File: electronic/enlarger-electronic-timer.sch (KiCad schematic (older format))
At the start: 1 part

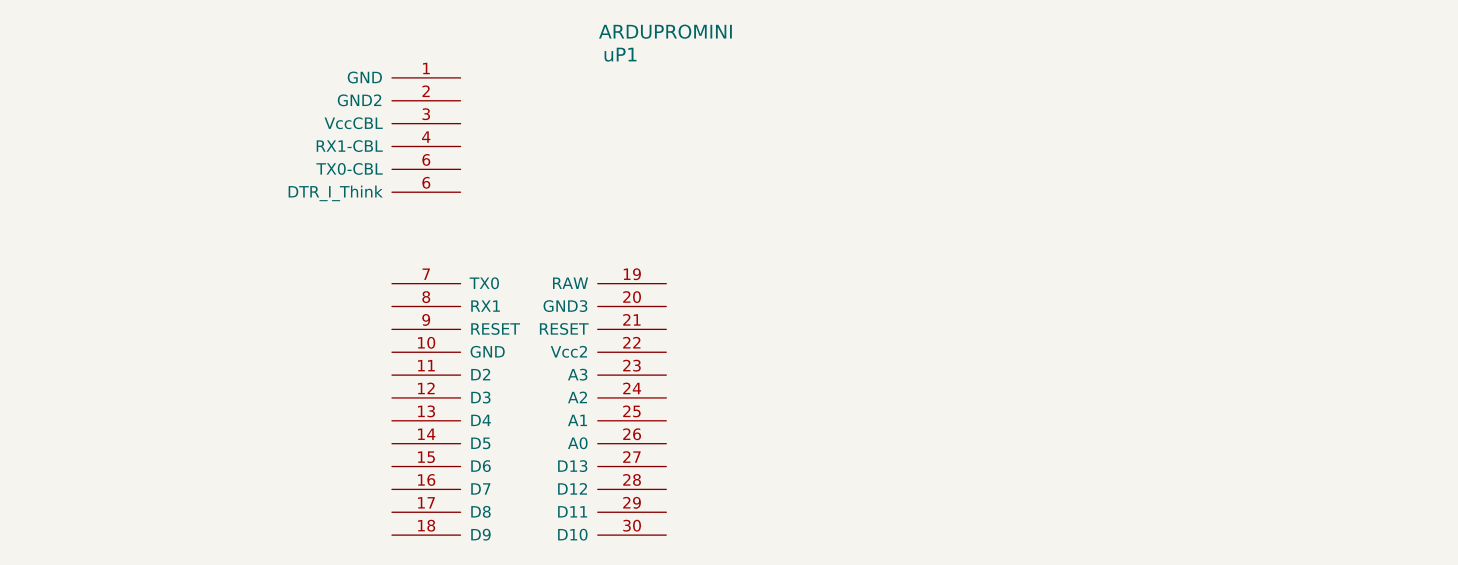
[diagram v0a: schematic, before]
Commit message: Fixed arduino library power pins, added grov connectors for relay/digits
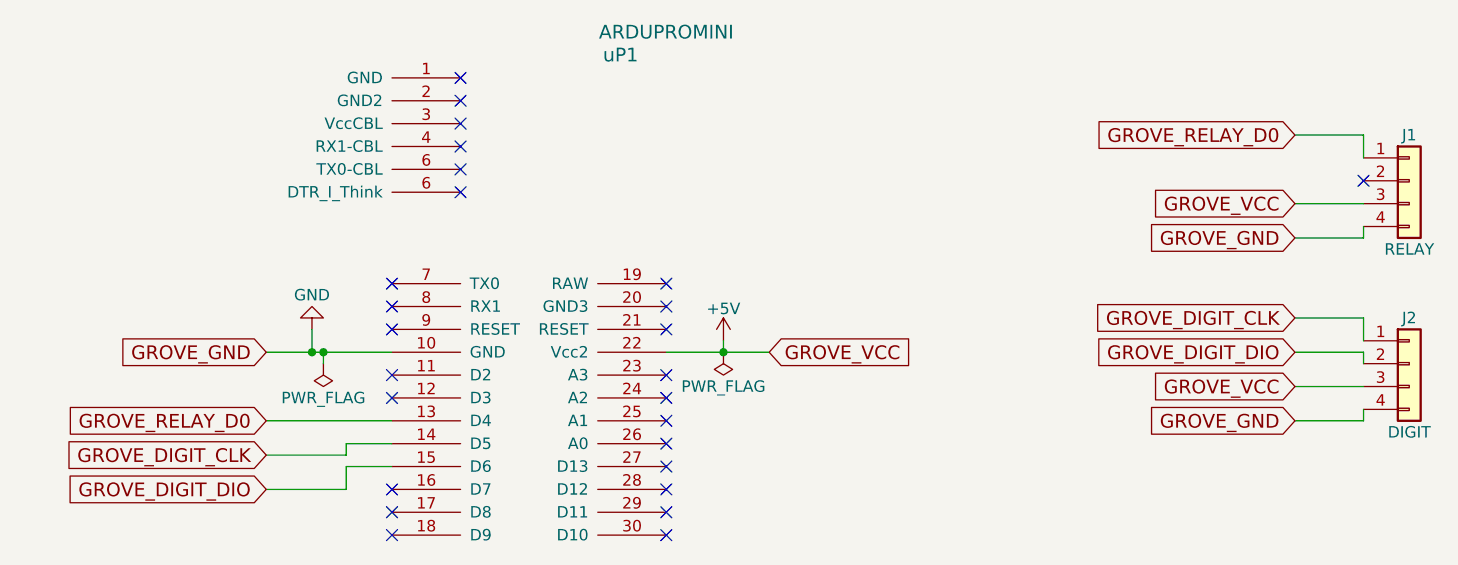
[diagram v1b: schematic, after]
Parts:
- added J1: RELAY, symbol Conn_01x04
- added J2: DIGIT, symbol Conn_01x04
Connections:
- net GND: now reaches uP1.10 (GND)
- net GND: now also J1.4 (Pin_4), J2.4 (Pin_4)
- net GROVE_RELAY_D0: now reaches uP1.13 (D4)
- net GROVE_RELAY_D0: now also J1.1 (Pin_1)
- net GROVE_DIGIT_CLK: now reaches uP1.14 (D5)
- net GROVE_DIGIT_CLK: now also J2.1 (Pin_1)
- net GROVE_DIGIT_DIO: now reaches uP1.15 (D6)
- net GROVE_DIGIT_DIO: now also J2.2 (Pin_2)
- net +5V: now reaches uP1.22 (Vcc2)
- net +5V: now also J1.3 (Pin_3), J2.3 (Pin_3)
- no-connect marks 0 -> 26
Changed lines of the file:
@@
 	1    0    0    -1
 $EndComp
+$Comp
+L Conn_01x04 J1
+U 1 1 5A3559CF
+P 6750 2600
+F 0 "J1" H 6750 2800 50  0000 C CNN
+F 1 "RELAY" H 6750 2300 50  0000 C CNN
+F 2 "" H 6750 2600 50  0001 C CNN
+F 3 "" H 6750 2600 50  0001 C CNN
+	1    6750 2600
+	1    0    0    -1
+$EndComp
+Text GLabel 6250 2400 0    60   Input ~ 0
+GROVE_RELAY_D0
+Text GLabel 6250 2700 0    60   Input ~ 0
+GROVE_VCC
+Text GLabel 6250 2850 0    60   Input ~ 0
+GROVE_GND
+Wire Wire Line
+	6250 2400 6550 2400
+Wire Wire Line
+	6550 2400 6550 2500
+Wire Wire Line
+	6250 2850 6550 2850
+Wire Wire Line
+	6550 2850 6550 2800
+Wire Wire Line
+	6250 2700 6550 2700
+Text GLabel 1750 3350 0    60   Input ~ 0
+GROVE_GND
+Wire Wire Line
+	2300 3350 1750 3350
+Text GLabel 3950 3350 2    60   Input ~ 0
+GROVE_VCC
+Text GLabel 1750 3650 0    60   Input ~ 0
+GROVE_RELAY_D0
+Wire Wire Line
+	1750 3650 2300 3650
+Wire Wire Line
+	3950 3350 3500 3350
+NoConn ~ 6550 2600
+$Comp
+L Conn_01x04 J2
+U 1 1 5A355E41
+P 6750 3400
+F 0 "J2" H 6750 3600 50  0000 C CNN
+F 1 "DIGIT" H 6750 3100 50  0000 C CNN
+F 2 "" H 6750 3400 50  0001 C CNN
+F 3 "" H 6750 3400 50  0001 C CNN
+	1    6750 3400
+	1    0    0    -1
+$EndComp
+Text GLabel 6250 3200 0    60   Input ~ 0
+GROVE_DIGIT_CLK
+Text GLabel 6250 3350 0    60   Input ~ 0
+GROVE_DIGIT_DIO
+Text GLabel 6250 3500 0    60   Input ~ 0
+GROVE_VCC
+Text GLabel 6250 3650 0    60   Input ~ 0
+GROVE_GND
+Wire Wire Line
+	6250 3200 6550 3200
+Wire Wire Line
+	6550 3200 6550 3300
+Wire Wire Line
+	6250 3350 6550 3350
+Wire Wire Line
+	6550 3350 6550 3400
+Wire Wire Line
+	6250 3500 6550 3500
+Wire Wire Line
+	6250 3650 6550 3650
+Wire Wire Line
+	6550 3650 6550 3600
+Text GLabel 1750 3800 0    60   Input ~ 0
+GROVE_DIGIT_CLK
+Text GLabel 1750 3950 0    60   Input ~ 0
+GROVE_DIGIT_DIO
+Wire Wire Line
+	1750 3950 2100 3950
+Wire Wire Line
+	2100 3950 2100 3850
+Wire Wire Line
+	2100 3850 2300 3850
+Wire Wire Line
+	1750 3800 2100 3800
+Wire Wire Line
+	2100 3800 2100 3750
+Wire Wire Line
+	2100 3750 2300 3750
+NoConn ~ 2600 2150
+NoConn ~ 2600 2250
+NoConn ~ 2600 2350
+NoConn ~ 2600 2450
+NoConn ~ 2600 2550
+NoConn ~ 2600 2650
+NoConn ~ 3500 3050
+NoConn ~ 3500 3150
+NoConn ~ 3500 3250
+NoConn ~ 3500 3450
+NoConn ~ 3500 3550
+NoConn ~ 3500 3650
+NoConn ~ 3500 3750
+NoConn ~ 3500 3850
+NoConn ~ 3500 3950
+NoConn ~ 3500 4050
+NoConn ~ 3500 4150
+NoConn ~ 2300 4150
+NoConn ~ 2300 4050
+NoConn ~ 2300 3950
+NoConn ~ 2300 3550
+NoConn ~ 2300 3450
+NoConn ~ 2300 3250
+NoConn ~ 2300 3150
+NoConn ~ 2300 3050
+$Comp
+L GND #PWR01
+U 1 1 5A356480
+P 1950 3250
+F 0 "#PWR01" H 1950 3000 50  0001 C CNN
+F 1 "GND" H 1950 3100 50  0000 C CNN
+F 2 "" H 1950 3250 50  0001 C CNN
+F 3 "" H 1950 3250 50  0001 C CNN
+	1    1950 3250
+	-1   0    0    1
+$EndComp
+Wire Wire Line
+	1950 3250 1950 3350
+Connection ~ 1950 3350
+$Comp
+L PWR_FLAG #FLG02
+U 1 1 5A3564BD
+P 2000 3400
+F 0 "#FLG02" H 2000 3475 50  0001 C CNN
+F 1 "PWR_FLAG" H 2000 3550 50  0000 C CNN
+F 2 "" H 2000 3400 50  0001 C CNN
+F 3 "" H 2000 3400 50  0001 C CNN
+	1    2000 3400
+	-1   0    0    1
+$EndComp
+Wire Wire Line
+	2000 3400 2000 3350
+Connection ~ 2000 3350
+$Comp
+L +5V #PWR03
+U 1 1 5A35653D
+P 3750 3300
+F 0 "#PWR03" H 3750 3150 50  0001 C CNN
+F 1 "+5V" H 3750 3440 50  0000 C CNN
+F 2 "" H 3750 3300 50  0001 C CNN
+F 3 "" H 3750 3300 50  0001 C CNN
+	1    3750 3300
+	1    0    0    -1
+$EndComp
+Wire Wire Line
+	3750 3300 3750 3350
+Connection ~ 3750 3350
+$Comp
+L PWR_FLAG #FLG04
+U 1 1 5A356577
+P 3750 3350
+F 0 "#FLG04" H 3750 3425 50  0001 C CNN
+F 1 "PWR_FLAG" H 3750 3500 50  0000 C CNN
+F 2 "" H 3750 3350 50  0001 C CNN
+F 3 "" H 3750 3350 50  0001 C CNN
+	1    3750 3350
+	-1   0    0    1
+$EndComp
 $EndSCHEMATC

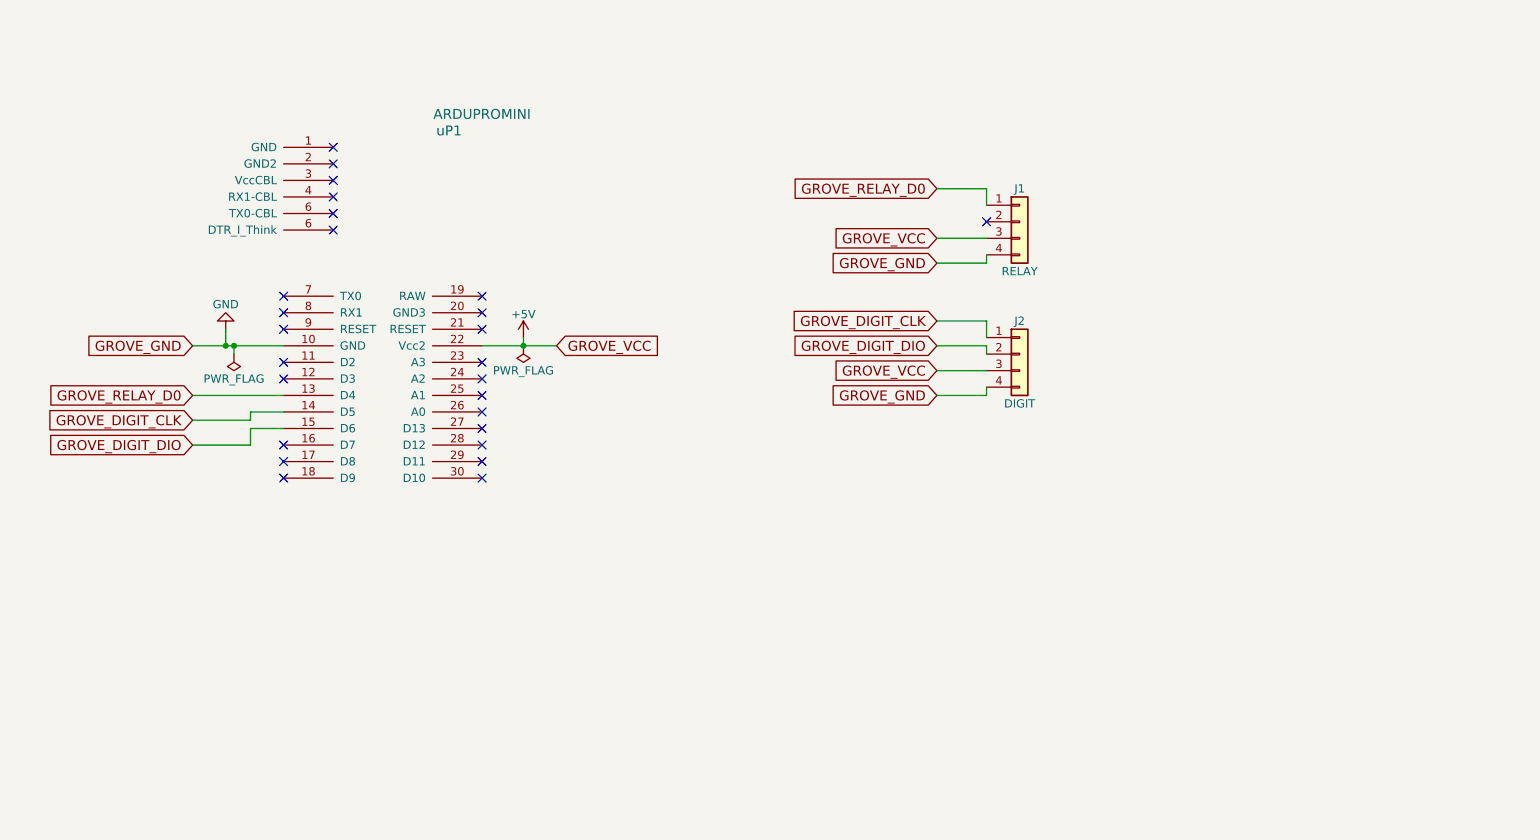
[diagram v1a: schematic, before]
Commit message: Added buttons, USB. placed components on PCB
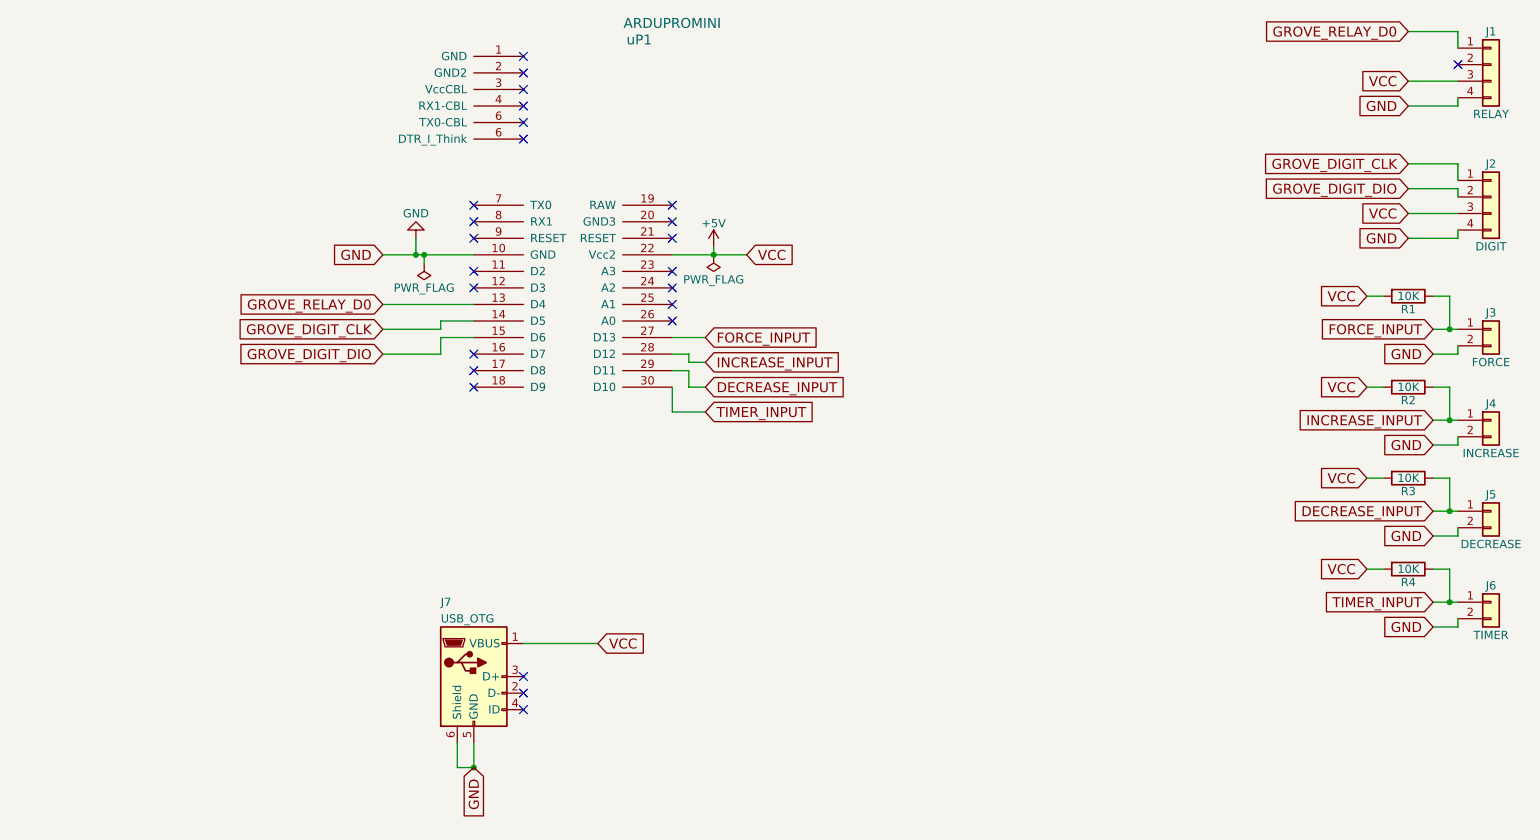
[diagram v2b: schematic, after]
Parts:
- added J3: FORCE, Pin_Headers:Pin_Header_Straight_1x02_Pitch2.54mm, symbol Conn_01x02
- added J4: INCREASE, Pin_Headers:Pin_Header_Straight_1x02_Pitch2.54mm, symbol Conn_01x02
- added J5: DECREASE, Pin_Headers:Pin_Header_Straight_1x02_Pitch2.54mm, symbol Conn_01x02
- added J6: TIMER, Pin_Headers:Pin_Header_Straight_1x02_Pitch2.54mm, symbol Conn_01x02
- added J7: USB_OTG, lib_fp:ST-USB-013A, symbol USB_OTG
- added R1, R2, R3, R4: 10K, Resistors_SMD:R_0603, symbol R
- J1, J2: footprint (none) -> Connectors:Grove_1x04
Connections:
- net +5V: now also J7.1 (VBUS), R1.2, R2.2, R3.2, R4.2
- net GND: now also J3.2 (Pin_2), J4.2 (Pin_2), J5.2 (Pin_2), J6.2 (Pin_2), J7.5 (GND), J7.6 (Shield)
- net FORCE_INPUT: now reaches uP1.27 (D13)
- net FORCE_INPUT: now also J3.1 (Pin_1), R1.1
- net INCREASE_INPUT: now reaches uP1.28 (D12)
- net INCREASE_INPUT: now also J4.1 (Pin_1), R2.1
- net DECREASE_INPUT: now reaches uP1.29 (D11)
- net DECREASE_INPUT: now also J5.1 (Pin_1), R3.1
- net TIMER_INPUT: now reaches uP1.30 (D10)
- net TIMER_INPUT: now also J6.1 (Pin_1), R4.1
- no-connect marks 26 -> 25
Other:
- moved on the sheet: J1, J2, uP1
